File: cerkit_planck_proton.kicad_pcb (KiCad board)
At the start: 2 copper layers, 251.5 x 128.3 mm, 103 parts

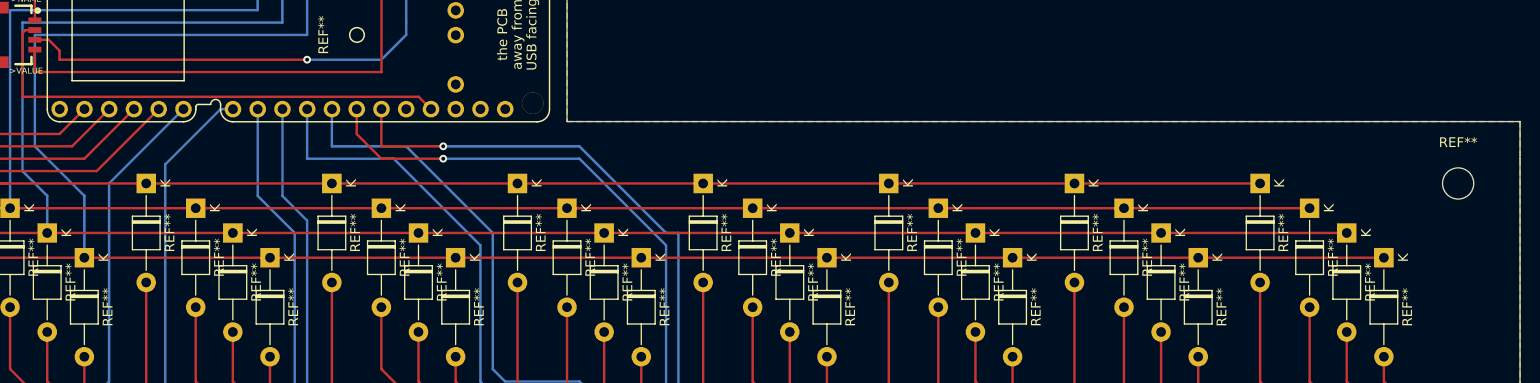
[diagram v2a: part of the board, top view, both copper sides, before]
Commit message: added reset button
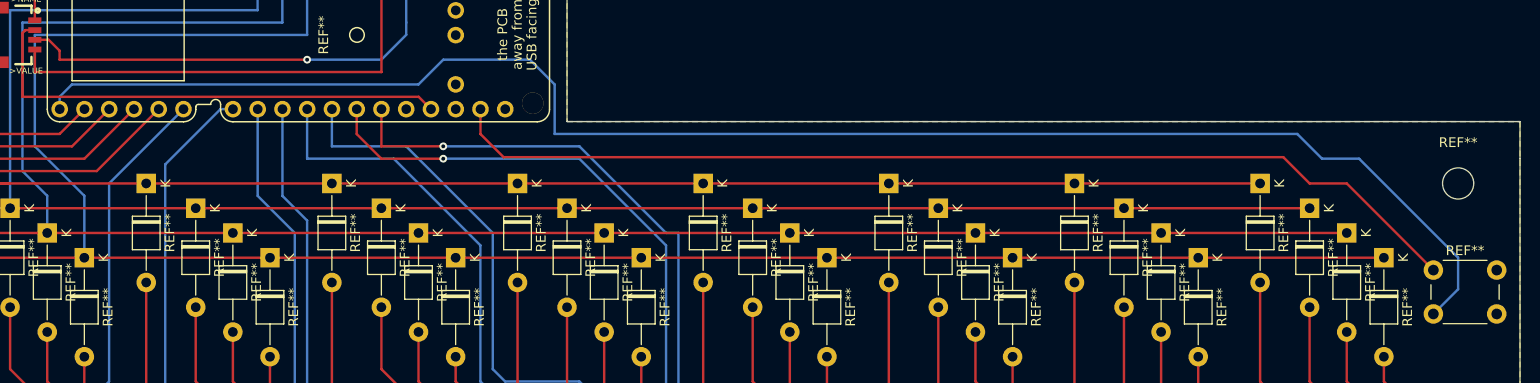
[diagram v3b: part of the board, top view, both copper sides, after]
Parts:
- added REF**: SW_PUSH_6mm, Button_Switch_THT:SW_PUSH_6mm, F.Cu at (261.6, 66.0)
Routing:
- net (no net): track 5138.9 -> 5409.6 mm
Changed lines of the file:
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@@
     (thickness 1.6)
     (drawings 10)
-    (tracks 574)
+    (tracks 593)
     (zones 0)
-    (modules 103)
+    (modules 104)
     (nets 1)
   )
@@
     (35 F.Paste user)
     (36 B.SilkS user hide)
-    (37 F.SilkS user)
+    (37 F.SilkS user hide)
     (38 B.Mask user)
     (39 F.Mask user)
@@
     (uvia_drill 0.1)
   )
+  (module Button_Switch_THT:SW_PUSH_6mm (layer F.Cu)
+    (at 261.62 66.04)
+    (descr https://www.omron.com/ecb/products/pdf/en-b3f.pdf)
+    (tags "tact sw push 6mm")
+    (fp_text reference REF** (at 3.25 -2) (layer F.SilkS)
+      (effects (font (size 1 1) (thickness 0.15)))
+    )
+    (fp_text value SW_PUSH_6mm (at 3.75 6.7) (layer F.Fab)
+      (effects (font (size 1 1) (thickness 0.15)))
+    )
+    (fp_text user %R (at 3.25 2.25) (layer F.Fab)
+      (effects (font (size 1 1) (thickness 0.15)))
+    )
+    (fp_line (start 3.25 -0.75) (end 6.25 -0.75) (layer F.Fab) (width 0.1))
+    (fp_line (start 6.25 -0.75) (end 6.25 5.25) (layer F.Fab) (width 0.1))
+    (fp_line (start 6.25 5.25) (end 0.25 5.25) (layer F.Fab) (width 0.1))
+    (fp_line (start 0.25 5.25) (end 0.25 -0.75) (layer F.Fab) (width 0.1))
+    (fp_line (start 0.25 -0.75) (end 3.25 -0.75) (layer F.Fab) (width 0.1))
+    (fp_line (start 7.75 6) (end 8 6) (layer F.CrtYd) (width 0.05))
+    (fp_line (start 8 6) (end 8 5.75) (layer F.CrtYd) (width 0.05))
+    (fp_line (start 7.75 -1.5) (end 8 -1.5) (layer F.CrtYd) (width 0.05))
+    (fp_line (start 8 -1.5) (end 8 -1.25) (layer F.CrtYd) (width 0.05))
+    (fp_line (start -1.5 -1.25) (end -1.5 -1.5) (layer F.CrtYd) (width 0.05))
+    (fp_line (start -1.5 -1.5) (end -1.25 -1.5) (layer F.CrtYd) (width 0.05))
+    (fp_line (start -1.5 5.75) (end -1.5 6) (layer F.CrtYd) (width 0.05))
+    (fp_line (start -1.5 6) (end -1.25 6) (layer F.CrtYd) (width 0.05))
+    (fp_line (start -1.25 -1.5) (end 7.75 -1.5) (layer F.CrtYd) (width 0.05))
+    (fp_line (start -1.5 5.75) (end -1.5 -1.25) (layer F.CrtYd) (width 0.05))
+    (fp_line (start 7.75 6) (end -1.25 6) (layer F.CrtYd) (width 0.05))
+    (fp_line (start 8 -1.25) (end 8 5.75) (layer F.CrtYd) (width 0.05))
+    (fp_line (start 1 5.5) (end 5.5 5.5) (layer F.SilkS) (width 0.12))
+    (fp_line (start -0.25 1.5) (end -0.25 3) (layer F.SilkS) (width 0.12))
+    (fp_line (start 5.5 -1) (end 1 -1) (layer F.SilkS) (width 0.12))
+    (fp_line (start 6.75 3) (end 6.75 1.5) (layer F.SilkS) (width 0.12))
+    (fp_circle (center 3.25 2.25) (end 1.25 2.5) (layer F.Fab) (width 0.1))
+    (pad 1 thru_hole circle (at 6.5 0 90) (size 2 2) (drill 1.1) (layers *.Cu *.Mask))
+    (pad 2 thru_hole circle (at 6.5 4.5 90) (size 2 2) (drill 1.1) (layers *.Cu *.Mask))
+    (pad 1 thru_hole circle (at 0 0 90) (size 2 2) (drill 1.1) (layers *.Cu *.Mask))
+    (pad 2 thru_hole circle (at 0 4.5 90) (size 2 2) (drill 1.1) (layers *.Cu *.Mask))
+    (model ${KISYS3DMOD}/Button_Switch_THT.3dshapes/SW_PUSH_6mm.wrl
+      (at (xyz 0 0 0))
+      (scale (xyz 1 1 1))
+      (rotate (xyz 0 0 0))
+    )
+  )
   (module Connectors:1X04_1MM_RA_STRESSRELIEF (layer F.Cu)
     (at 118.11 41.91 270)
@@
   (segment (start 161.3 34.31) (end 161.3 33.03) (width 0.25) (layer F.Cu) (net 0))
   (segment (start 161.3 33.03) (end 161.29 33.02) (width 0.25) (layer F.Cu) (net 0))
-  (segment (start 161.29 33.02) (end 118.11 33.02) (width 0.25) (layer F.Cu) (net 0))
   (segment (start 118.11 33.02) (end 118.11 40.4114) (width 0.25) (layer F.Cu) (net 0))
   (segment (start 117.151083 41.41216) (end 118.11 41.41216) (width 0.25) (layer F.Cu) (net 0))
@@
   (segment (start 119.531038 42.40784) (end 118.11 42.40784) (width 0.25) (layer F.Cu) (net 0))
   (segment (start 120.65 43.526802) (end 119.531038 42.40784) (width 0.25) (layer F.Cu) (net 0))
+  (segment (start 161.29 33.02) (end 118.11 33.02) (width 0.25) (layer F.Cu) (net 0))
+  (segment (start 163.84 49.525) (end 163.84 52.08) (width 0.25) (layer F.Cu) (net 0))
+  (segment (start 166.214666 54.454666) (end 246.224666 54.454666) (width 0.25) (layer F.Cu) (net 0))
+  (segment (start 163.84 52.08) (end 166.214666 54.454666) (width 0.25) (layer F.Cu) (net 0))
+  (segment (start 246.224666 54.454666) (end 248.92 57.15) (width 0.25) (layer F.Cu) (net 0))
+  (segment (start 252.73 57.15) (end 261.62 66.04) (width 0.25) (layer F.Cu) (net 0))
+  (segment (start 248.92 57.15) (end 252.73 57.15) (width 0.25) (layer F.Cu) (net 0))
+  (segment (start 264.16 68) (end 261.62 70.54) (width 0.25) (layer B.Cu) (net 0))
+  (segment (start 264.16 64.77) (end 264.16 68) (width 0.25) (layer B.Cu) (net 0))
+  (segment (start 157.48 46.99) (end 160.02 44.45) (width 0.25) (layer B.Cu) (net 0))
+  (segment (start 120.66 49.525) (end 120.66 48.25) (width 0.25) (layer B.Cu) (net 0))
+  (segment (start 250.19 54.61) (end 254 54.61) (width 0.25) (layer B.Cu) (net 0))
+  (segment (start 168.91 44.45) (end 171.45 46.99) (width 0.25) (layer B.Cu) (net 0))
+  (segment (start 121.92 46.99) (end 157.48 46.99) (width 0.25) (layer B.Cu) (net 0))
+  (segment (start 247.65 52.07) (end 250.19 54.61) (width 0.25) (layer B.Cu) (net 0))
+  (segment (start 171.45 46.99) (end 171.45 52.07) (width 0.25) (layer B.Cu) (net 0))
+  (segment (start 171.45 52.07) (end 247.65 52.07) (width 0.25) (layer B.Cu) (net 0))
+  (segment (start 160.02 44.45) (end 168.91 44.45) (width 0.25) (layer B.Cu) (net 0))
+  (segment (start 120.66 48.25) (end 121.92 46.99) (width 0.25) (layer B.Cu) (net 0))
+  (segment (start 254 54.61) (end 264.16 64.77) (width 0.25) (layer B.Cu) (net 0))
   (zone (net 0) (net_name "") (layer F.Cu) (hatch edge 0.508)
     (connect_pads (clearance 0.508))
